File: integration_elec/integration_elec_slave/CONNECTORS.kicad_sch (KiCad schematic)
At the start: 0 parts

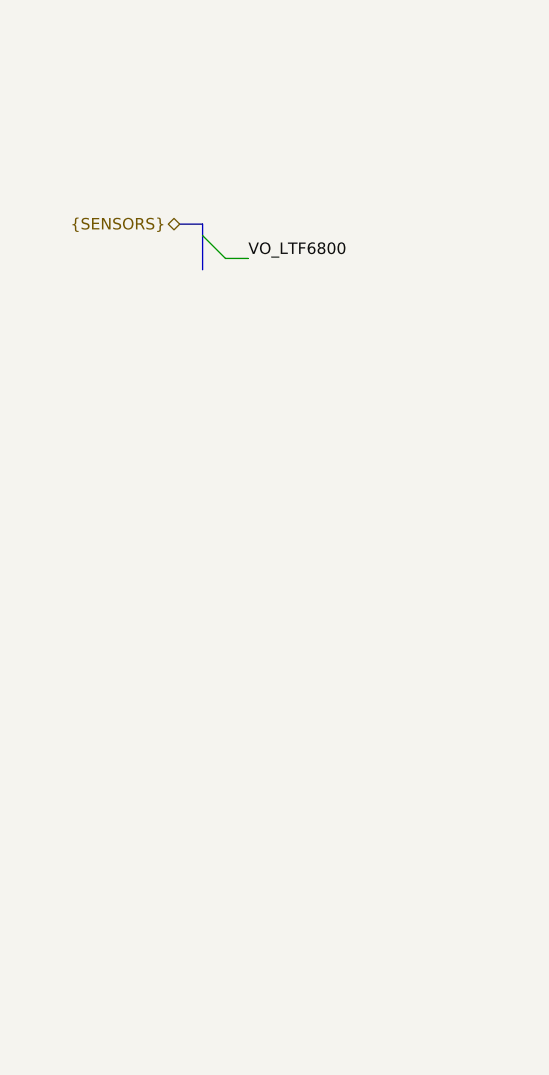
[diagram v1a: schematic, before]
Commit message: EM - Correction des bus
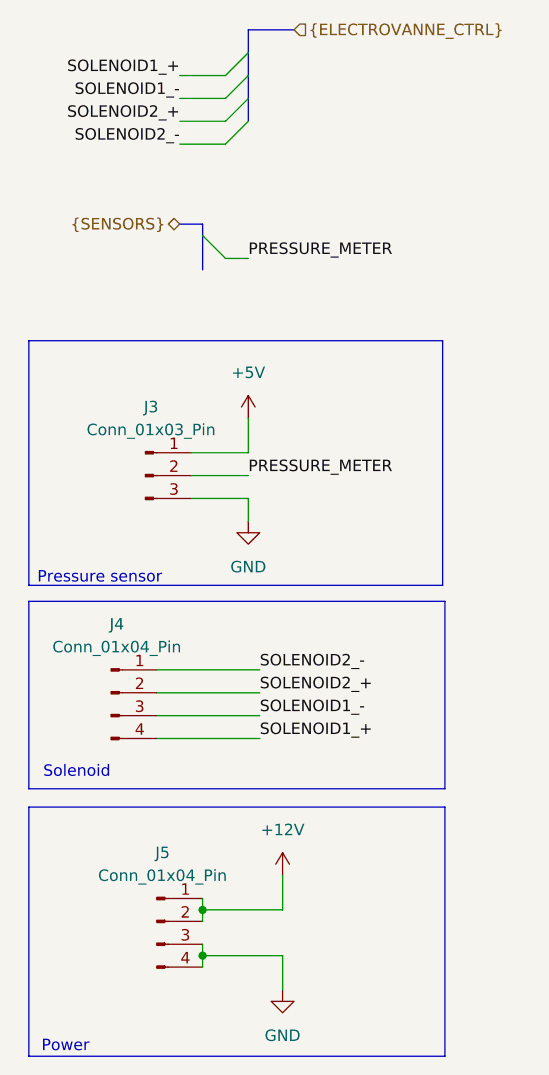
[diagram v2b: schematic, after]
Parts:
- added J3: Conn_01x03_Pin, symbol Connector:Conn_01x03_Pin
- added J4, J5: Conn_01x04_Pin, symbol Connector:Conn_01x04_Pin
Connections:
- new net +12V: J5.1 (Pin_1), J5.2 (Pin_2)
- new net +5V: J3.1 (Pin_1)
- new net GND: J3.3 (Pin_3), J5.3 (Pin_3), J5.4 (Pin_4)
- new net PRESSURE_METER: J3.2 (Pin_2)
- new net SOLENOID1_+: J4.4 (Pin_4)
- new net SOLENOID1_-: J4.3 (Pin_3)
- new net SOLENOID2_+: J4.2 (Pin_2)
- new net SOLENOID2_-: J4.1 (Pin_1)
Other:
- note added: "Power"
- note added: "Pressure sensor"
- note added: "Solenoid"

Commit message: EM - Fini schématique attente de review
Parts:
- J3: footprint (none) -> Connector_Molex:Molex_Micro-Fit_3.0_43650-0315_1x03_P3.00mm_Vertical; DigiKey (none) -> 538-43650-0315
- J4, J5: footprint (none) -> Connector_Molex:Molex_Micro-Fit_3.0_43650-0415_1x04_P3.00mm_Vertical; DigiKey (none) -> WM1919-ND
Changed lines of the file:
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@@
 			)
 		)
-		(property "Footprint" ""
+		(property "Footprint" "Connector_Molex:Molex_Micro-Fit_3.0_43650-0415_1x04_P3.00mm_Vertical"
 			(at 30.48 111.76 0)
 			(effects
@@
 		)
 		(property "Description" "Generic connector, single row, 01x04, script generated"
+			(at 30.48 111.76 0)
+			(effects
+				(font
+					(size 1.27 1.27)
+				)
+				(hide yes)
+			)
+		)
+		(property "DigiKey" "WM1919-ND"
 			(at 30.48 111.76 0)
 			(effects
@@
 			)
 		)
-		(property "Footprint" ""
+		(property "Footprint" "Connector_Molex:Molex_Micro-Fit_3.0_43650-0315_1x03_P3.00mm_Vertical"
 			(at 34.29 87.63 0)
 			(effects
@@
 		)
 		(property "Description" "Generic connector, single row, 01x03, script generated"
+			(at 34.29 87.63 0)
+			(effects
+				(font
+					(size 1.27 1.27)
+				)
+				(hide yes)
+			)
+		)
+		(property "DigiKey" "538-43650-0315 "
 			(at 34.29 87.63 0)
 			(effects
@@
 			)
 		)
-		(property "Footprint" ""
+		(property "Footprint" "Connector_Molex:Molex_Micro-Fit_3.0_43650-0415_1x04_P3.00mm_Vertical"
 			(at 35.56 137.16 0)
 			(effects
@@
 			(at 35.56 137.16 0)
 			(effects
+				(font
+					(size 1.27 1.27)
+				)
+				(hide yes)
+			)
+		)
+		(property "DigiKey" "WM1919-ND"
+			(at 35.56 137.16 0)
+			(effects
